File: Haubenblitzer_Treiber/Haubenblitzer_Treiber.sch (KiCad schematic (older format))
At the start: 40 parts, among them J1 ISCP, J2 Micro_USB, J3 Screw_Terminal_01x02, J4 Screw_Terminal_01x03, J5 Screw_Terminal_01x05, J6 RJ12, J7 RJ12, Q1 MMBT3906, Q2 MMBT3906, U1 ATmega32U4-AU, U2 NCV8460, U3 3021-D-E-1000, U4 3021-D-E-1000, Y1 Crystal

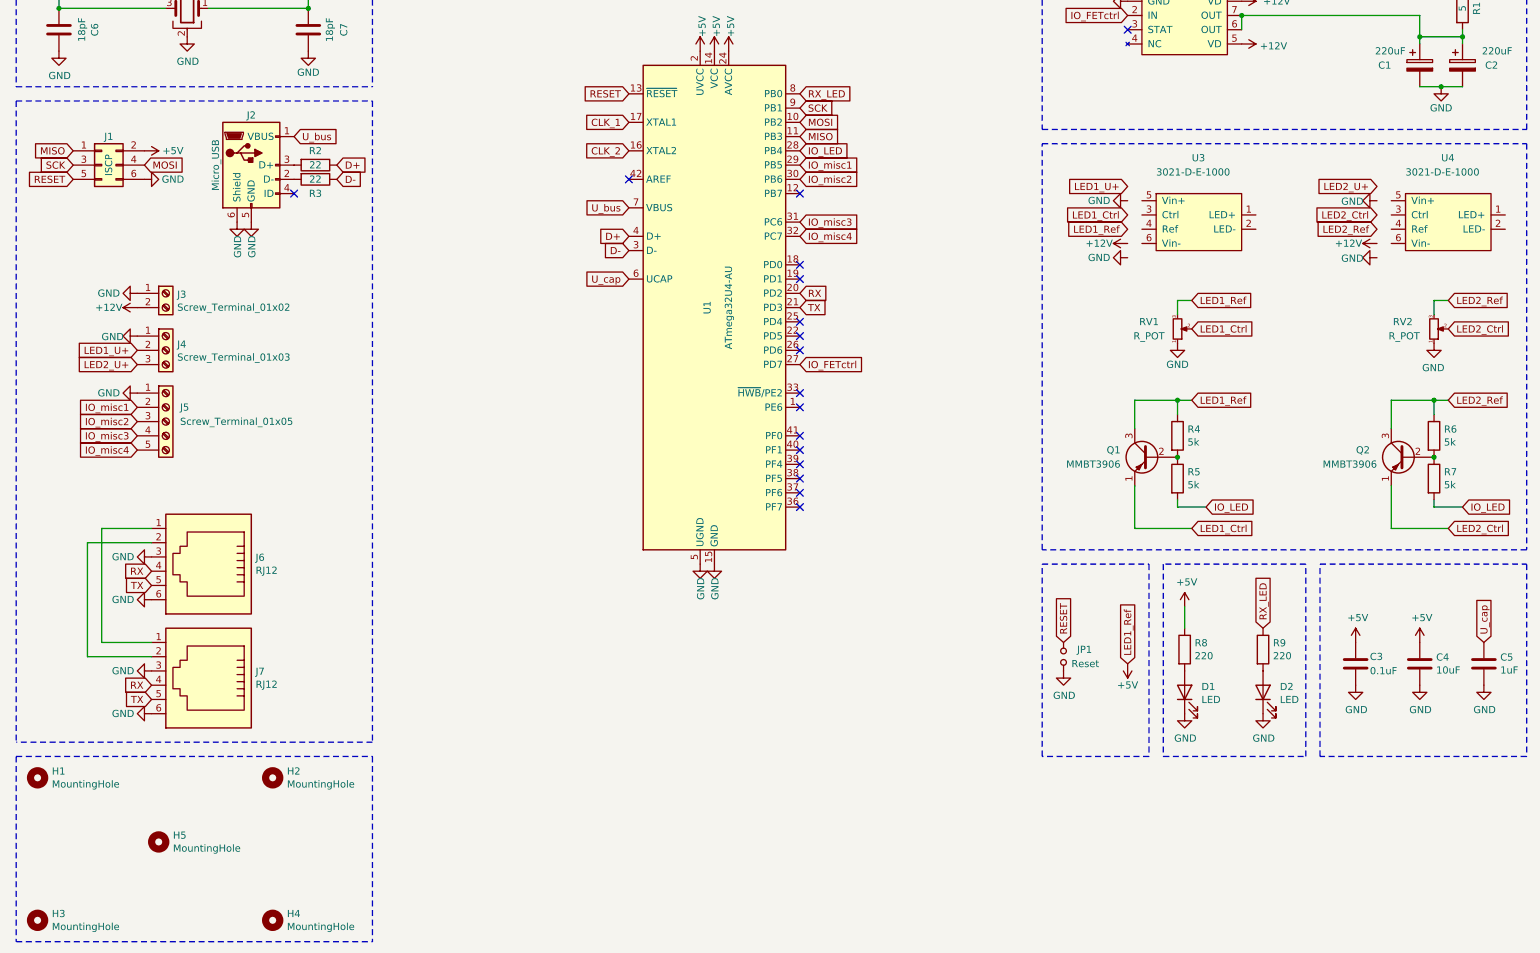
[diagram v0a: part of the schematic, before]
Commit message: added ESD protection and gerber files
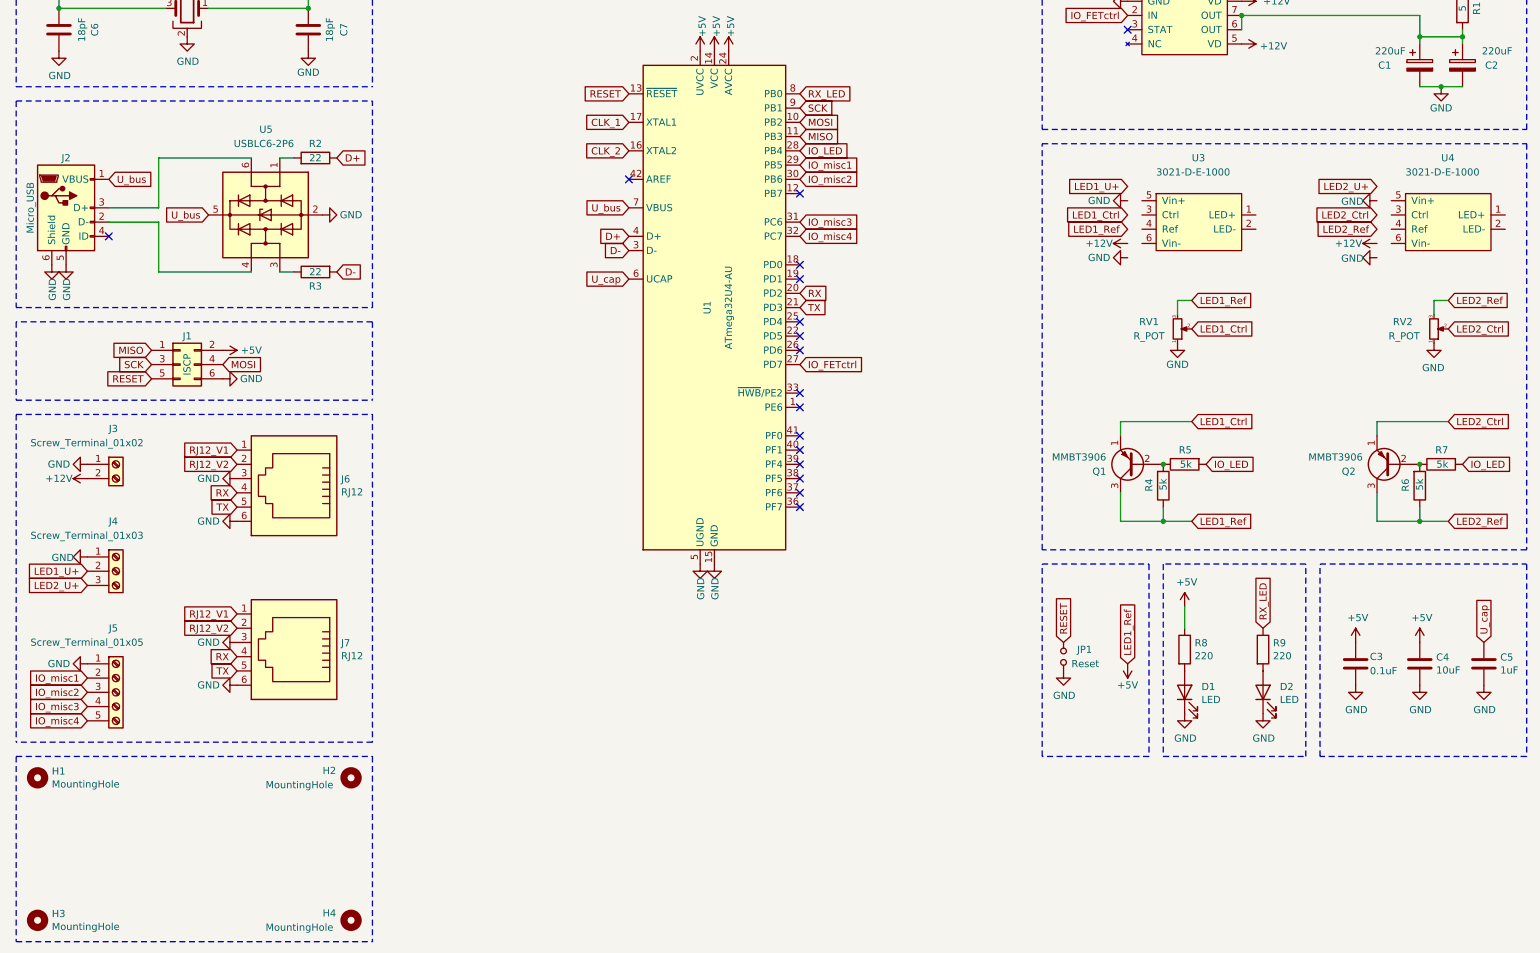
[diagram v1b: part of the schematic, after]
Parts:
- removed H5: MountingHole, MountingHole:MountingHole_3.2mm_M3, symbol Mechanical:MountingHole
- added U5: USBLC6-2P6, Package_TO_SOT_SMD:SOT-23-6, symbol Power_Protection:USBLC6-2P6
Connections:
- net D-: now also R3.2; no longer R3.1
- net GND: now also U5.2 (GND)
- net U_bus: now also U5.5 (VBUS)
- net RJ12_V1: now reaches J6.1, J7.1
- net RJ12_V2: now reaches J6.2, J7.2
- net at R2.2: now also U5.1 (I/O1); no longer J2.3 (D+)
- net at J2.2 (D-): now also U5.4 (I/O2); no longer R3.2
- new net: R3.1, U5.3 (I/O2)
- new net: J2.3 (D+), U5.6 (I/O1)
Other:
- moved on the sheet: H2, H4, J1, J2, J3, J4, J5, J6, J7, Q1, Q2, R2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

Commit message: Version2.0
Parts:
- removed C1, C2: 220uF, Capacitor_SMD:CP_Elec_10x10, symbol Device:CP
- removed C7: 18pF, Capacitor_SMD:C_0805_2012Metric, symbol Device:C
- removed J2: Micro_USB, Connector_USB:USB_Micro-B_GCT_USB3076-30-A, symbol Connector:USB_B_Micro
- removed JP1: Reset, Jumper:SolderJumper-2_P1.3mm_Open_RoundedPad1.0x1.5mm, symbol Device:Jumper_NO_Small
- removed Q1, Q2: MMBT3906, Package_TO_SOT_SMD:SA1162, symbol Transistor_BJT:2N3906
- removed R2: 22, Resistor_SMD:R_0805_2012Metric, symbol Device:R
- removed U1: ATmega32U4-AU, Package_QFP:TQFP-44_10x10mm_P0.8mm, symbol MCU_Microchip_ATmega:ATmega32U4-AU
- removed U2: NCV8460, Package_SO:SOIC-8_3.9x4.9mm_P1.27mm, symbol Power_Management:NCV8460
- removed U5: USBLC6-2P6, Package_TO_SOT_SMD:SOT-23-6, symbol Power_Protection:USBLC6-2P6
- added C1: 1uF, Capacitor_SMD:C_0805_2012Metric, symbol Device:C
- added C2: 4.7uF, Capacitor_SMD:C_0805_2012Metric, symbol Device:C
- added C3, C4: 220uF, Capacitor_SMD:CP_Elec_10x10, symbol Device:CP
- added C6: 18pF, Capacitor_SMD:C_0805_2012Metric, symbol Device:C_Small
- added J7: USB_C_4510, Connector_USB:USB_C_4510, symbol Interface_USB:USB_C_4510
- added JP1, JP6: Jumper, Jumper:SolderJumper-2_P1.3mm_Open_Pad2.0x4.0mm, symbol Jumper:SolderJumper_2_Open
- added JP2, JP3: Jumper, Jumper:SolderJumper-3_P1.3mm_Open_RoundedPad1.0x1.5mm, symbol Jumper:SolderJumper_3_Open
- added JP4, JP5: Jumper, Jumper:SolderJumper-2_P1.3mm_Open_RoundedPad1.0x1.5mm, symbol Jumper:SolderJumper_2_Open
- added Q1, Q2: IRF7205, Package_SO:SOIC-8_IRF7205, symbol Transistor_FET:BS250
- added Q3, Q4: AO3401A, Package_TO_SOT_SMD:SOT-23, symbol Transistor_FET:AO3401A
- added R10: 1K, Resistor_SMD:R_0805_2012Metric, symbol Device:R
- added R11: 5K, Resistor_SMD:R_0805_2012Metric, symbol Device:R
- added R12, R8, R9: 5k, Resistor_SMD:R_0805_2012Metric, symbol Device:R
- added R14, R17: 5.1K, Resistor_SMD:R_0805_2012Metric, symbol Device:R
- added R15, R16: 22, Resistor_SMD:R_0805_2012Metric, symbol Device:R
- added U1: LDL1117S50R, Package_TO_SOT_SMD:SOT-223, symbol Regulator_Linear:AMS1117-5.0
- added U4: ATmega16U4-AU, Package_DFN_QFN:QFN-44-1EP_7x7mm_P0.5mm_EP5.2x5.2mm, symbol MCU_Microchip_ATmega:ATmega16U4-AU
- C5: renamed from C6; symbol Device:C -> Device:C_Small
- J1: renamed from J3; value Screw_Terminal_01x02 -> Screw_Terminal
- J2: renamed from J4; value Screw_Terminal_01x03 -> Screw_Terminal
- J4: renamed from J5; value Screw_Terminal_01x05 -> Screw_Terminal
- R1: value 5 -> 10k; footprint Resistor_SMD:MP725 -> Resistor_SMD:R_0805_2012Metric; Shop https://www.digikey.de/product-detail/de/caddock-electronic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 -> (none)
- R3: value 22 -> 5; footprint Resistor_SMD:R_0805_2012Metric -> Package_TO_SOT_SMD:PAK-2
- R4: value 5k -> 10k
- R5, R6: value 5k -> 200
- R7: value 5k -> 5K
- RV1, RV2: footprint Potentiometer_SMD:Potentiometer_Vishay_TS53YJ_Vertical -> Potentiometer_SMD:Potentiometer_ACP_PS10_Vertical_Hole
- renumbered C5 to C7, C3 to C8, C4 to C9, J1 to J3, J6 to J5, J7 to J6, R9 to R13, R8 to R2, U3 to U2, U4 to U3
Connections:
- net +12V is gone; now on net VCC: J1.2 (Pin_2), R1.1
- net LED1_U+ is gone; now on net U_LED1: J2.2 (Pin_2)
- net LED2_U+ is gone; now on net U_LED2: J2.3 (Pin_3)
- net +5V: now also U2.4 (Ref), C2.2, Q3.2 (S), U1.2 (VO), U4.14 (VCC), U4.2 (UVCC), U4.24 (AVCC), U4.34 (VCC), U4.44 (AVCC); no longer R4.1
- net CLK_1: now also U4.17 (XTAL1)
- net CLK_2: now also C6.2, U4.16 (XTAL2)
- net D+: now also R15.2, U4.4 (D+)
- net D-: now also R16.2, U4.3 (D-); no longer R3.2
- net GND: now also R7.2, U2.2 (LED-), U2.6 (Vin-), U3.2 (LED-), U3.6 (Vin-), C1.1, C2.1, C3.2, C4.2, C6.1, J7.A1, J7.A12, J7.B1, J7.B12, J7.GND, R10.2, R11.2, R12.2, R14.2, R17.2, R8.2, R9.2, U1.1 (GND), U4.15 (GND), U4.23 (GND), U4.35 (GND), U4.43 (GND), U4.5 (UGND); no longer J2.1 (Pin_1), RV1.1, RV2.1
- net IO_LED: now also R4.2, R5.1, R6.1, Q2.2 (G), U4.32 (PC7); no longer R5.2, R7.2
- net MISO: now also U4.11 (PB3)
- net MOSI: now also U4.10 (PB2)
- net RESET: now also U4.13 (~RESET)
- net RX: now also U4.20 (PD2)
- net SCK: now also U4.9 (PB1)
- net TX: now also U4.21 (PD3)
- net VCC: now reaches R3.1
- net VCC: now also C1.2, JP1.1 (A), Q1.3 (S), U1.3 (VI)
- net U_LED1: now reaches U2.1 (LED+)
- net U_LED1: now also JP6.1 (A), Q2.1 (D)
- net LED1_CTRL: now reaches U2.3 (Ctrl)
- net LED1_CTRL: now also JP2.2 (C), Q3.3 (D)
- net U_Driver: now reaches U2.5 (Vin+)
- net U_Driver: now also R3.2, R4.1, U3.5 (Vin+), C3.1, C4.1, JP1.2 (B), Q1.1 (D), Q2.3 (S)
- net U_LED2: now reaches U3.1 (LED+)
- net U_LED2: now also JP6.2 (B)
- net LED2_CTRL: now reaches U3.3 (Ctrl)
- net LED2_CTRL: now also JP3.2 (C), Q4.3 (D)
- net LED2_REF: now reaches U3.4 (Ref)
- net LED2_REF: now also RV2.3, Q4.2 (S)
- net IO_BRIDGE_INRUSH_R: now reaches R1.2
- net IO_BRIDGE_INRUSH_R: now also Q1.2 (G), U4.18 (PD0)
- net at R7.1: now also JP4.2 (B); no longer R6.2
- net IO_misc1 renamed IO_MISC1
- net IO_MISC1: now also U4.28 (PB4)
- net IO_misc2 renamed IO_MISC2
- net IO_MISC2: now also U4.29 (PB5)
- net IO_misc3 renamed IO_MISC3
- net IO_MISC3: now also U4.30 (PB6)
- net IO_misc4 renamed IO_MISC4
- net IO_MISC4: now also U4.31 (PC6)
- net LED1_Ctrl: no longer names the net of RV1.2
- net LED1_Ctrl: now also JP2.1 (A)
- net LED2_Ctrl: no longer names the net of RV2.2
- net LED2_Ctrl: now also JP3.1 (A)
- removed net LED2_Ref: R6.1, RV2.3
- net RX_LED: no longer names the net of R13.1
- net RX_LED: now also U4.19 (PD1)
- net U_cap: no longer names the net of C7.2
- net U_cap: now also U4.6 (UCAP)
- new net: JP4.1 (A), RV1.1
- new net: Q3.1 (G), R5.2, R9.1
- new net: JP5.1 (A), RV2.1
- new net: Q4.1 (G), R12.1, R6.2
- new net: JP3.3 (B), R11.1
- new net: JP2.3 (B), R8.1
- new net: J7.A5, R14.1
- new net: J7.A6, R15.1
- new net: J7.A7, R16.1
- new net: J7.B5, R17.1
- new net: JP5.2 (B), R10.1
- new net GND_LED: J2.1 (Pin_1)
- new net VBUS: J7.A4, J7.A9, J7.B4, J7.B9, U4.7 (VBUS)
- no-connect marks 17 -> 19
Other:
- note added: "1-2: I_VARIABLE\n2-3: I_MAX"
- note added: "5V Voltage via:"
- note added: "CLOSED: V_LED1 = V_LED2\n(ONLY FOR I_MAX & DIRECT MODE)"
- note added: "Clock"
- note added: "DIRECT (MOSFET)"
- note added: "DRIVER (BUCK)"
- note added: "Driver IC"
- note added: "I/O\n"
- note added: "ISCP"
- note added: "Input 8-18V"
- note added: "LED CONTROLLER"
- note added: "LED1"
- note added: "LED2"
- note added: "Linear Regulator"
- note added: "MODES:\n- DIRECT (U1&Q2): 6:C\n- DRIVER (U2&U3): 1:O\n - I_VARIABLE: 2:12, 4:C, 6:O\n - I_MAX: 2:23, 4:0, 6:C\n\n? : Doesn't matter\nO: OPEN\nC: CLOSED\n"
- note added: "Overcurrent Protection"
- note added: "RJ12 Connectors"
- note added: "Screw Terminals"
- note added: "U LED CTRL"
- note added: "USB-C Port"
- note added: "disable inrush\ncurrent protection"
- note added: "https://tinyurl.com/ydbvc5ak"
- note added: "https://www.falstad.com/circuit/circuitjs.html?ctz=CQAgjCAMB0l3BWcMBMcUHYMGZIA4UA2ATmIxAUgpABZsKBTAWjDACgA3cQkbBFbiDxURtKklEwEbMBhogUNKmGIC0eBUvDJ4UaHjCFh8E-AgAlBgGcAllYAuAQwB2AYwZsATkKopFP3n4ocEpINgAHbl9-Qyo+AQgRNgB3APjBdLDU4UCEwjigrIC-eViFfzDvRV8EHmrc4LB4FIV8cvlceRKoFvqczoCigf7IUpp5IdHwDB4B7qL69IHMrwaloLLxZqsxZXzaQlL95RAAM0cAGysPVOxsWaD1gUn5fvvBtgAPWjB6NCRxsRWhouvIAPIAOS+vGIPDAKCB41K2AEoJAYIAYh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"
- note added: "uController"
- moved on the sheet: C5, C7, C8, C9, D1, D2, H2, J1, J2, J3, J4, J5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
